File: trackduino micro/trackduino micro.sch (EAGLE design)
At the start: 28 parts, among them IC2 74AHC1G125DBV, SW1 SPST_TACT-KMR2, U1 ATMEGA168, Y1 16MHZ

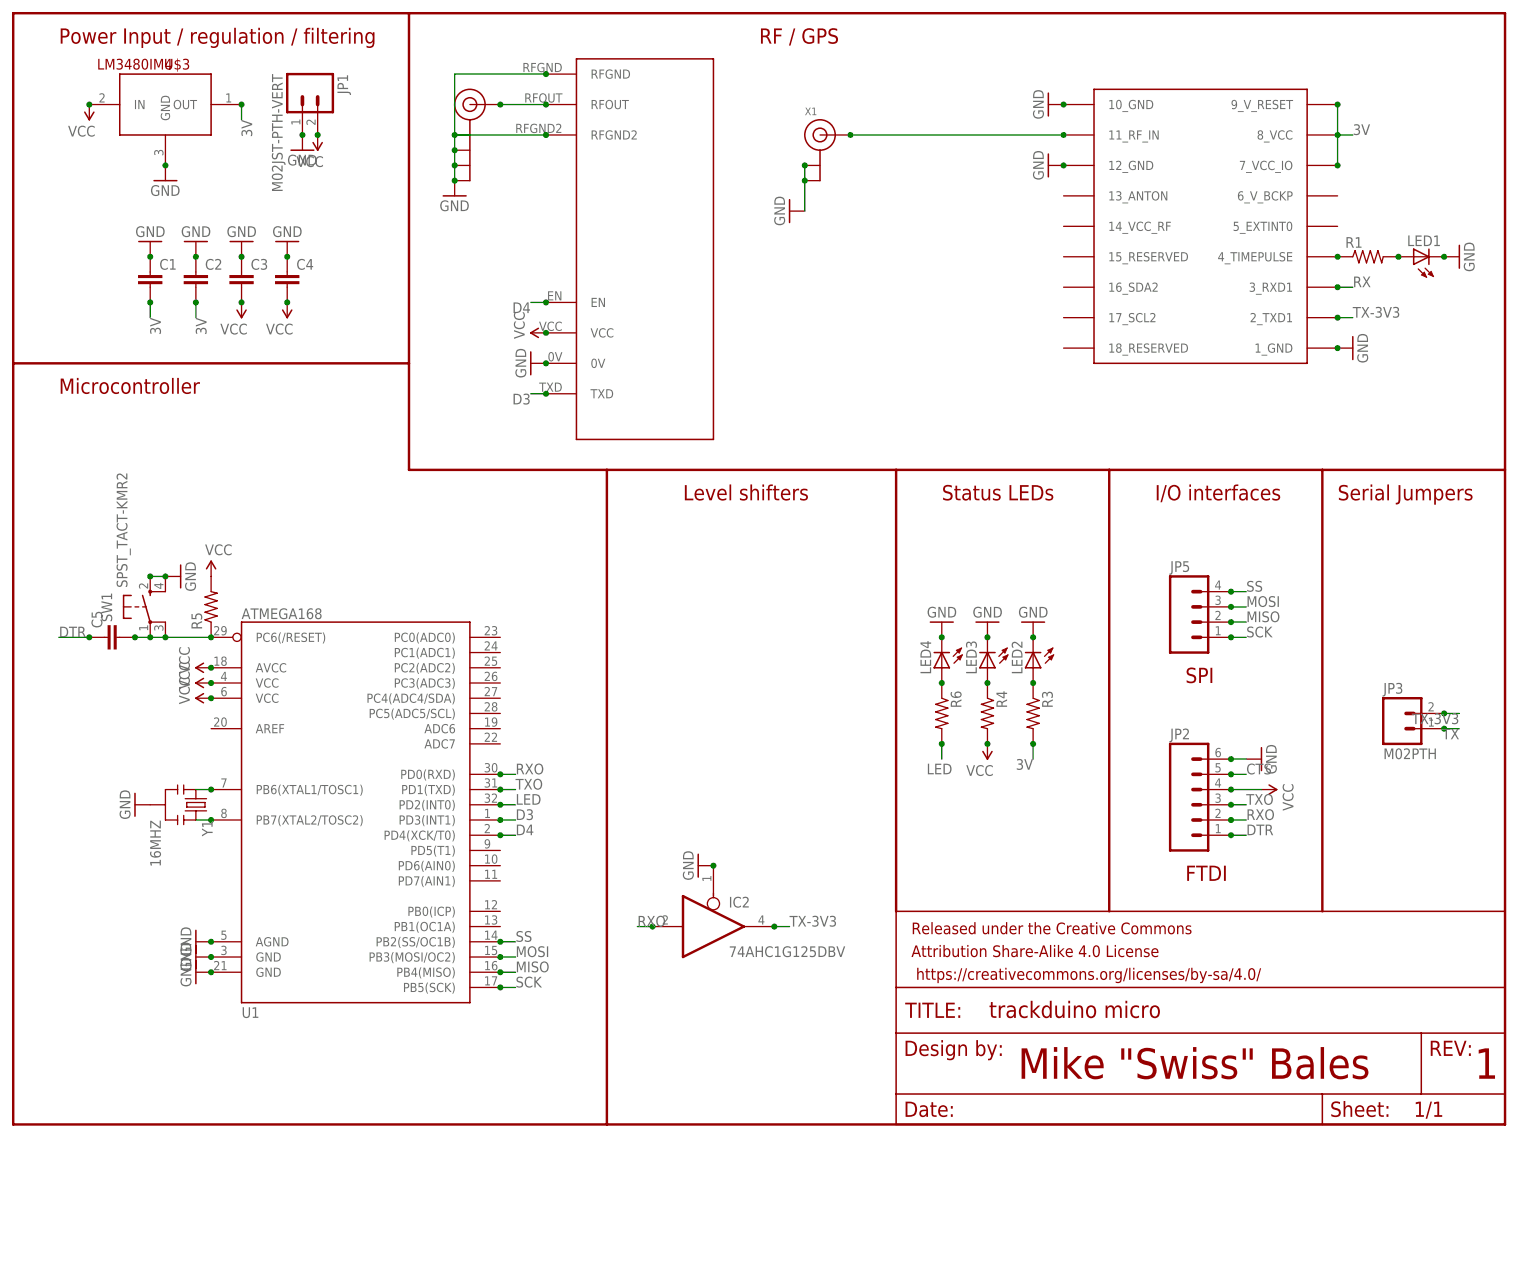
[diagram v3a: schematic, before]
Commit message: fixed consistency error on last commit
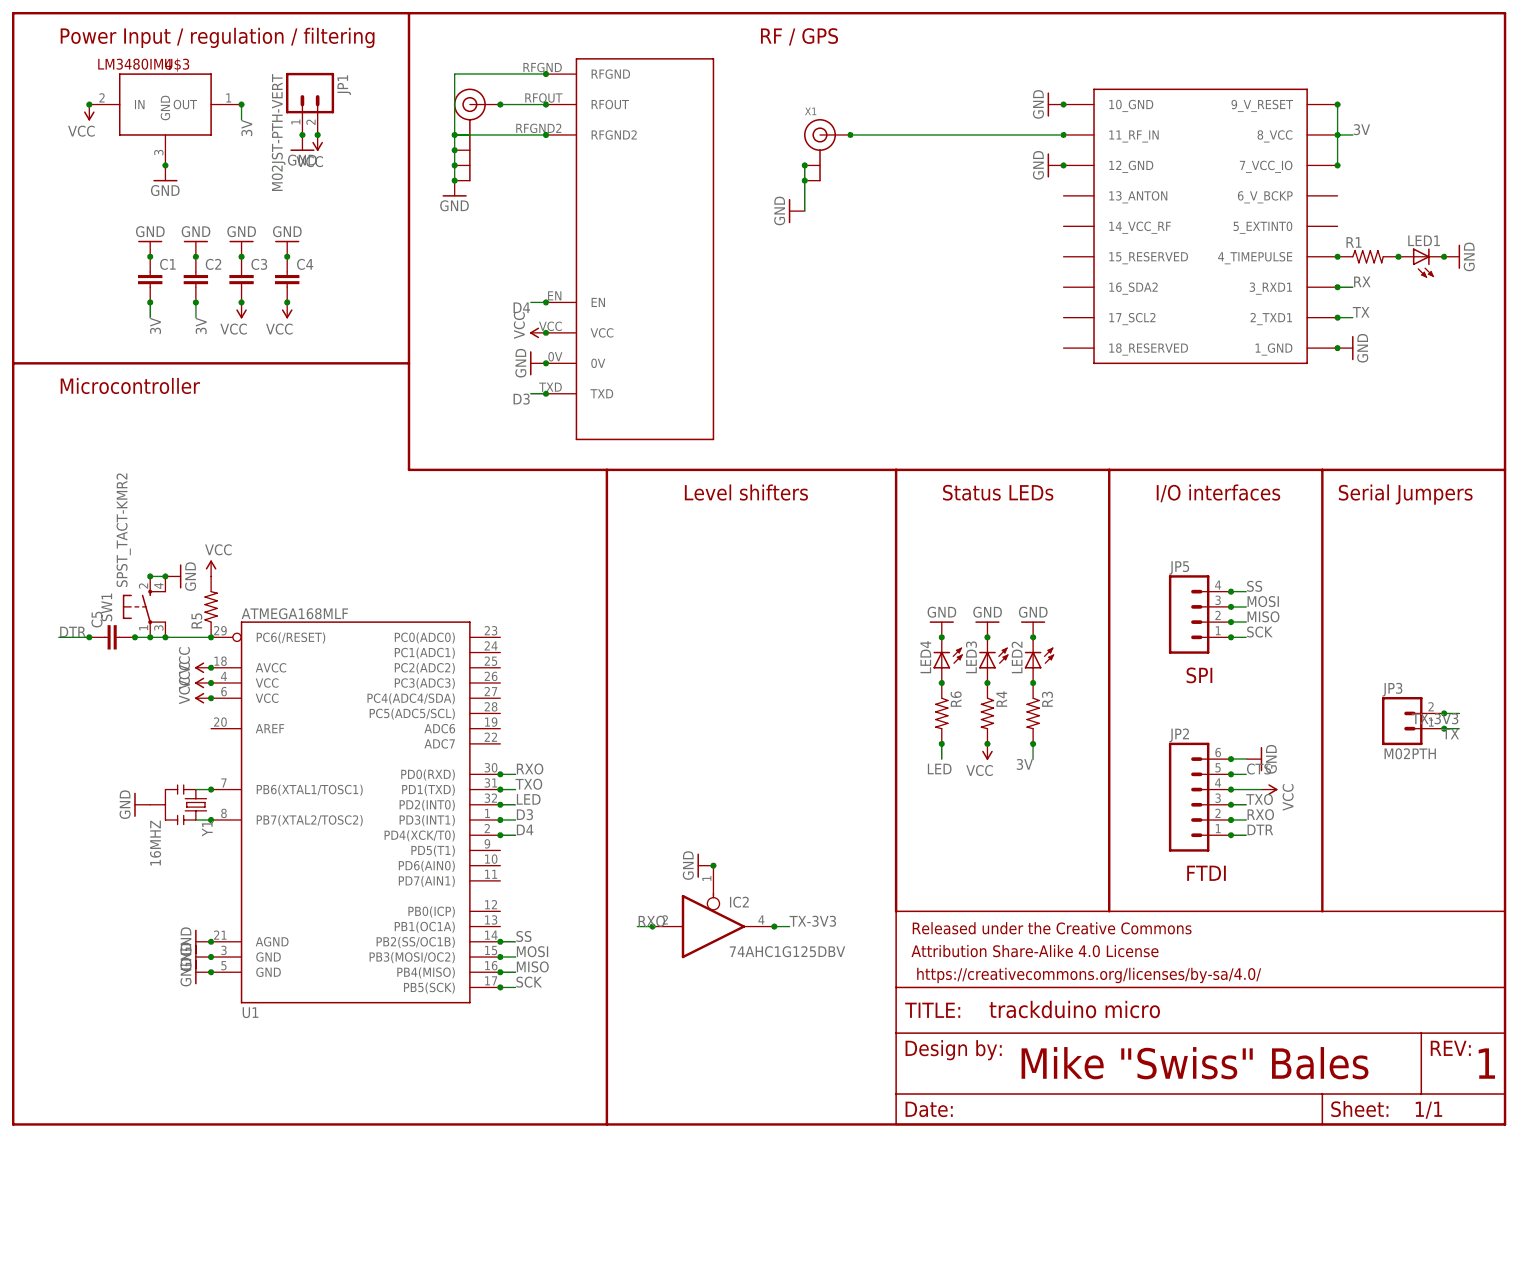
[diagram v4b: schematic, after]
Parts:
- U1: value ATMEGA168 -> ATMEGA168MLF; device SparkFun-DigitalIC:ATMEGA168 -> SparkFun-DigitalIC:ATMEGA168MLF
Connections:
- net TX: now also U$1.2_TXD1
- net TX-3V3: no longer U$1.2_TXD1
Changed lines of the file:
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@@
 <parts>
 <part name="IC2" library="74xx-little-us" deviceset="74*1G125" device="DBV" technology="AHC"/>
-<part name="U1" library="SparkFun-DigitalIC" deviceset="ATMEGA168" device="" value="ATMEGA168"/>
+<part name="U1" library="SparkFun-DigitalIC" deviceset="ATMEGA168" device="MLF" value="ATMEGA168MLF"/>
 <part name="U$2" library="Ava" deviceset="RADIOMETRIX-HX1" device=""/>
 <part name="U$3" library="SparkFun-PowerIC" deviceset="LM3480IM4" device=""/>
@@
 <part name="GND5" library="SparkFun-Aesthetics" deviceset="GND" device=""/>
 <part name="SUPPLY1" library="SparkFun-Aesthetics" deviceset="VCC" device=""/>
-<part name="GND6" library="SparkFun-Aesthetics" deviceset="GND" device=""/>
 <part name="SUPPLY2" library="SparkFun-Aesthetics" deviceset="VCC" device=""/>
 <part name="SUPPLY3" library="SparkFun-Aesthetics" deviceset="VCC" device=""/>
@@
 <part name="C4" library="SparkFun-Capacitors" deviceset="CAP" device="0805"/>
 <part name="GND15" library="SparkFun-Aesthetics" deviceset="GND" device=""/>
-<part name="GND16" library="SparkFun-Aesthetics" deviceset="GND" device=""/>
 <part name="GND17" library="SparkFun-Aesthetics" deviceset="GND" device=""/>
 <part name="GND18" library="SparkFun-Aesthetics" deviceset="GND" device=""/>
@@
 <part name="X1" library="adafruit" deviceset="ANTENNA_U.FL" device=""/>
 <part name="SW1" library="adafruit" deviceset="SPST_TACT" device="-KMR2"/>
+<part name="GND1" library="SparkFun-Aesthetics" deviceset="GND" device=""/>
+<part name="GND3" library="SparkFun-Aesthetics" deviceset="GND" device=""/>
 </parts>
 <sheets>
@@
 <instance part="GND5" gate="1" x="48.26" y="162.56"/>
 <instance part="SUPPLY1" gate="G$1" x="50.8" y="165.1" rot="R180"/>
-<instance part="GND6" gate="1" x="25.4" y="157.48"/>
 <instance part="SUPPLY2" gate="G$1" x="12.7" y="170.18" rot="R180"/>
 <instance part="SUPPLY3" gate="G$1" x="88.9" y="132.08" rot="R90"/>
@@
 <instance part="C4" gate="G$1" x="45.72" y="139.7"/>
 <instance part="GND15" gate="1" x="22.86" y="147.32" rot="R180"/>
-<instance part="GND16" gate="1" x="30.48" y="147.32" rot="R180"/>
 <instance part="GND17" gate="1" x="38.1" y="147.32" rot="R180"/>
 <instance part="GND18" gate="1" x="45.72" y="147.32" rot="R180"/>
@@
 <instance part="X1" gate="G$1" x="134.62" y="165.1"/>
 <instance part="SW1" gate="G$1" x="22.86" y="86.36"/>
+<instance part="GND1" gate="1" x="30.48" y="147.32" rot="R180"/>
+<instance part="GND3" gate="1" x="25.4" y="157.48"/>
 </instances>
 <busses>
@@
 </segment>
 <segment>
-<pinref part="U$3" gate="G$1" pin="GND"/>
-<pinref part="GND6" gate="1" pin="GND"/>
-<junction x="25.4" y="160.02"/>
-</segment>
-<segment>
 <pinref part="JP1" gate="G$1" pin="1"/>
 <pinref part="GND5" gate="1" pin="GND"/>
@@
 </segment>
 <segment>
-<pinref part="C2" gate="G$1" pin="1"/>
-<pinref part="GND16" gate="1" pin="GND"/>
-<junction x="30.48" y="144.78"/>
-</segment>
-<segment>
 <pinref part="C3" gate="G$1" pin="1"/>
 <pinref part="GND17" gate="1" pin="GND"/>
@@
 <junction x="220.98" y="129.54"/>
 </segment>
+<segment>
+<pinref part="C2" gate="G$1" pin="1"/>
+<pinref part="GND1" gate="1" pin="GND"/>
+<junction x="30.48" y="144.78"/>
+</segment>
+<segment>
+<pinref part="U$3" gate="G$1" pin="GND"/>
+<pinref part="GND3" gate="1" pin="GND"/>
+<junction x="25.4" y="160.02"/>
+</segment>
 </net>
 <net name="TX-3V3" class="0">
@@
 <junction x="238.76" y="68.58"/>
 </segment>
+</net>
+<net name="D3" class="0">
+<segment>
+<pinref part="U1" gate="G$1" pin="PD3(INT1)"/>
+<wire x1="81.28" y1="50.8" x2="83.82" y2="50.8" width="0.1524" layer="91"/>
+<label x="83.82" y="50.8" size="1.778" layer="95"/>
+<junction x="81.28" y="50.8"/>
+</segment>
+<segment>
+<pinref part="U$2" gate="G$1" pin="TXD"/>
+<wire x1="88.9" y1="121.92" x2="86.36" y2="121.92" width="0.1524" layer="91"/>
+<label x="86.36" y="121.92" size="1.778" layer="95" rot="R180"/>
+<junction x="88.9" y="121.92"/>
+</segment>
+</net>
+<net name="TX" class="0">
+<segment>
+<pinref part="JP3" gate="G$1" pin="1"/>
+<wire x1="238.76" y1="66.04" x2="241.3" y2="66.04" width="0.1524" layer="91"/>
+<label x="241.3" y="66.04" size="1.778" layer="95" rot="R180"/>
+<junction x="238.76" y="66.04"/>
+</segment>
 <segment>
 <wire x1="220.98" y1="134.62" x2="223.52" y2="134.62" width="0.1524" layer="91"/>
@@
 </segment>
 </net>
-<net name="D3" class="0">
-<segment>
-<pinref part="U1" gate="G$1" pin="PD3(INT1)"/>
-<wire x1="81.28" y1="50.8" x2="83.82" y2="50.8" width="0.1524" layer="91"/>
-<label x="83.82" y="50.8" size="1.778" layer="95"/>
-<junction x="81.28" y="50.8"/>
-</segment>
-<segment>
-<pinref part="U$2" gate="G$1" pin="TXD"/>
-<wire x1="88.9" y1="121.92" x2="86.36" y2="121.92" width="0.1524" layer="91"/>
-<label x="86.36" y="121.92" size="1.778" layer="95" rot="R180"/>
-<junction x="88.9" y="121.92"/>
-</segment>
-</net>
-<net name="TX" class="0">
-<segment>
-<pinref part="JP3" gate="G$1" pin="1"/>
-<wire x1="238.76" y1="66.04" x2="241.3" y2="66.04" width="0.1524" layer="91"/>
-<label x="241.3" y="66.04" size="1.778" layer="95" rot="R180"/>
-<junction x="238.76" y="66.04"/>
-</segment>
-</net>
